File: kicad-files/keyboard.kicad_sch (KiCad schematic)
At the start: 180 parts, among them J1 TYPE-C-31-M12_13, Q1 2N7002, Q2 2N7002, SW1 K2-1187SQ-A4SW-06, U1 STM32F411CEU6, U2 USBLC6-2SC6, U3 AT24C256C-SSHL-T, U4 SGM2007-3.3XN5/TR, Y1 TAXM8M4RFDCET2T

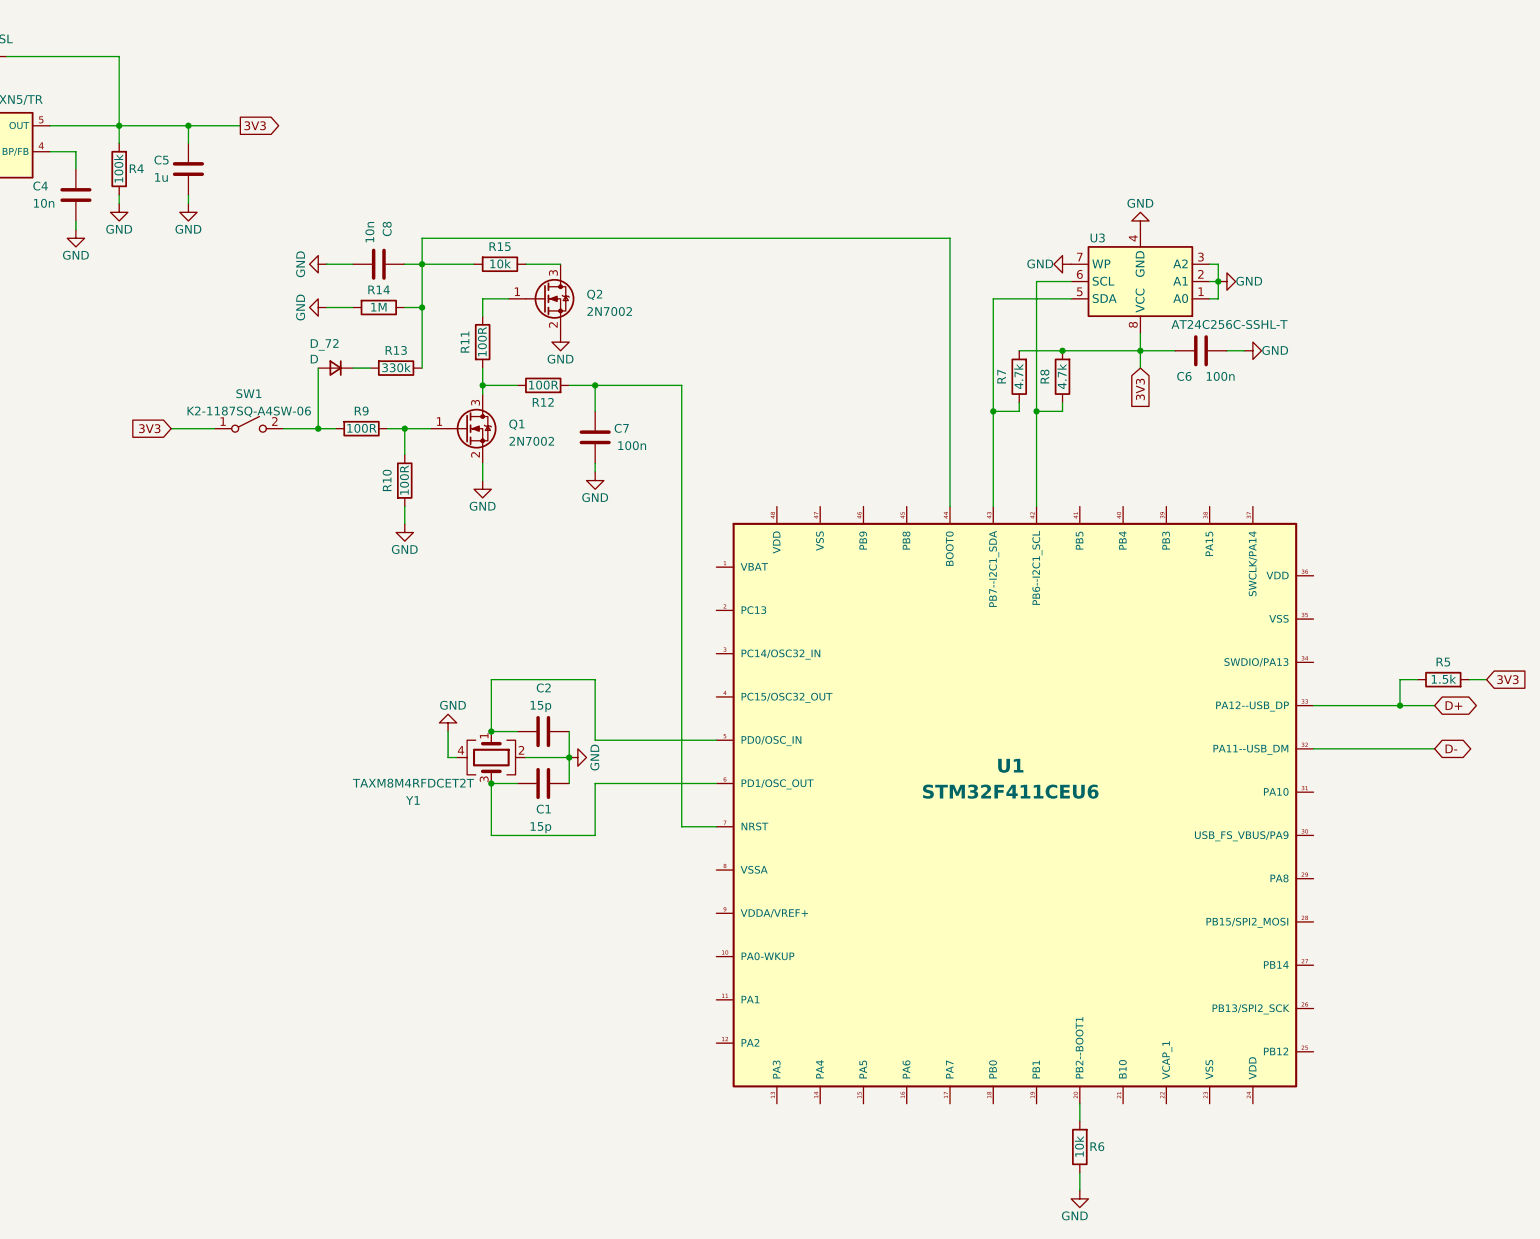
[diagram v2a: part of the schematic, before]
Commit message: Added 3V3 connections to controller
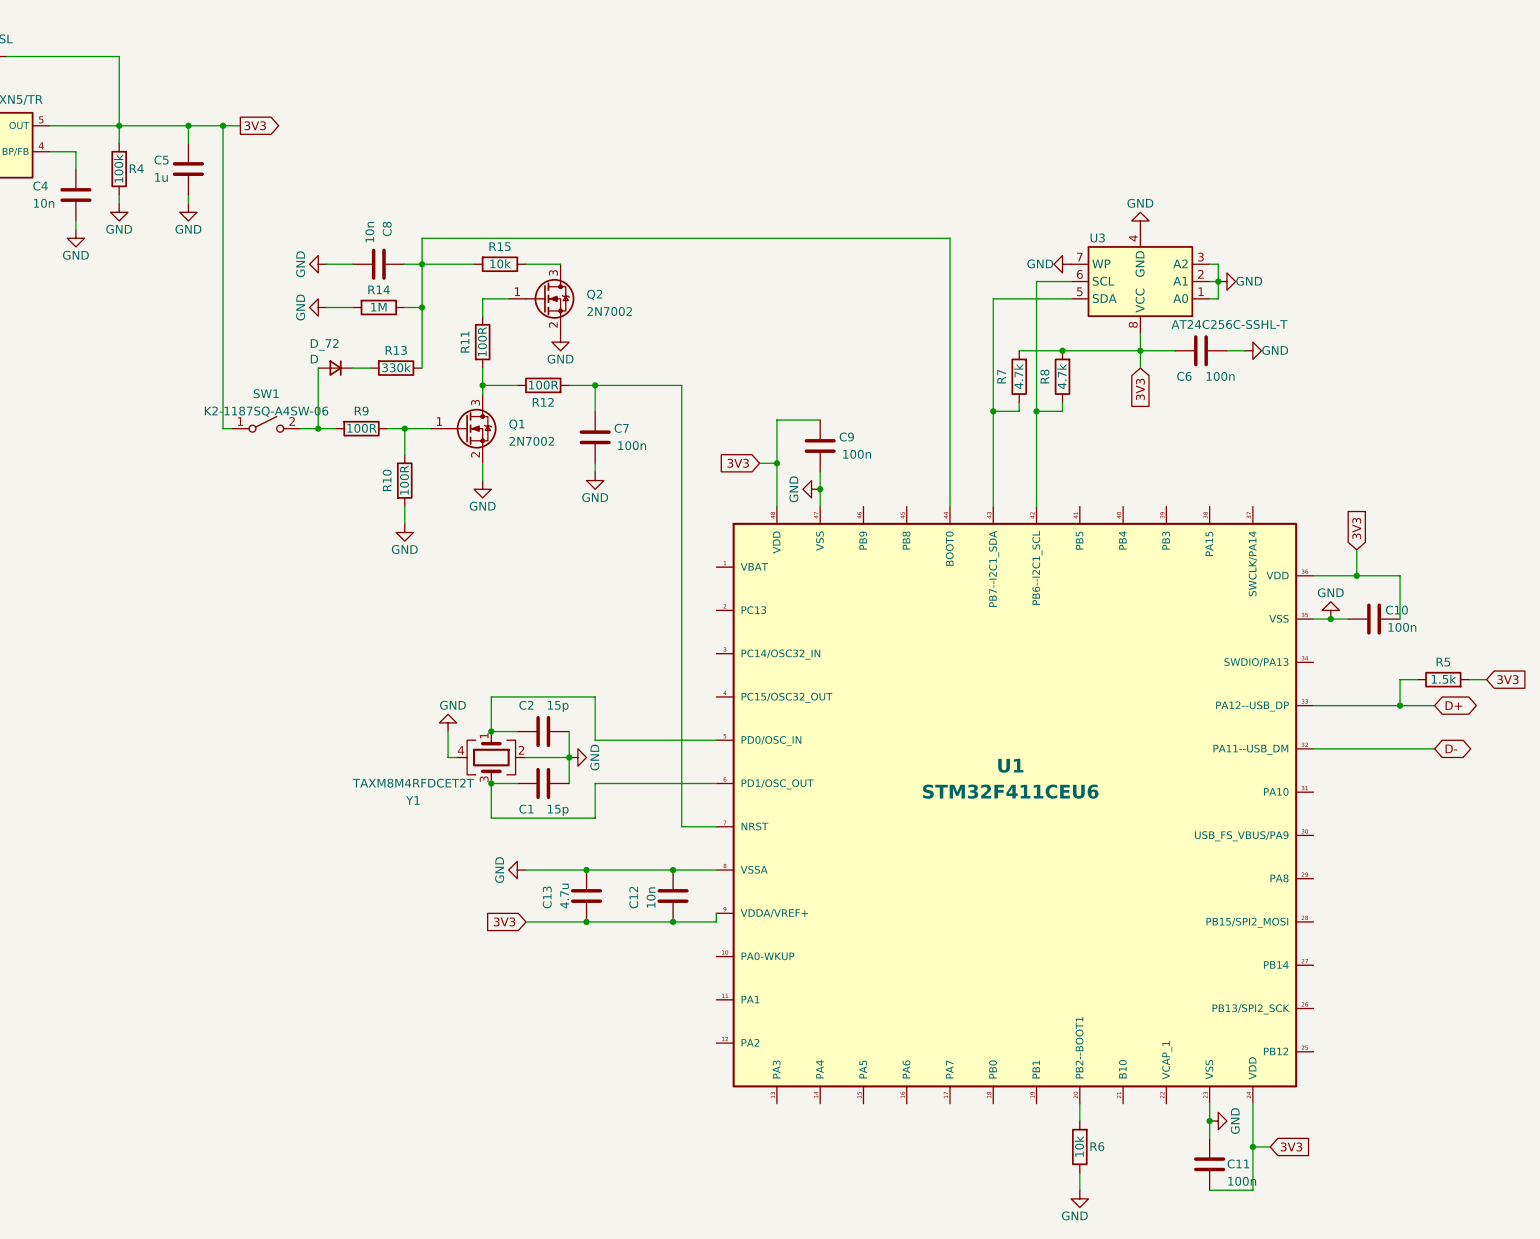
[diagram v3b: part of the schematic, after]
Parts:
- added C10, C11, C9: 100n, Capacitor_SMD:C_0603_1608Metric_Pad1.08x0.95mm_HandSolder, symbol Device:C
- added C12: 10n, Capacitor_SMD:C_0603_1608Metric_Pad1.08x0.95mm_HandSolder, symbol Device:C
- added C13: 4.7u, Capacitor_SMD:C_0603_1608Metric_Pad1.08x0.95mm_HandSolder, symbol Device:C
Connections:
- net 3V3: now also U1.24 (VDD), U1.36 (VDD), U1.48 (VDD), U1.9 (VDDA/VREF+), C10.2, C11.2, C12.2, C13.2, C9.2
- net GND: now also U1.23 (VSS), U1.35 (VSS), U1.47 (VSS), U1.8 (VSSA), C10.1, C11.1, C12.1, C13.1, C9.1
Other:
- moved on the sheet: SW1

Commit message: Connected pulldown for 3V3 on the STM
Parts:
- U1: footprint acheron_Components:STM_UFQFPN-48_LQFP-48-1EP_7x7mm_P0.5mm_HandSoldering_ThermalReliefs -> acheron_Components:STM_UFQFPN-48_LQFP-48-1EP_7x7mm_P0.5mm_HandSoldering
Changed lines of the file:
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@@
       (effects (font (size 2.0066 2.0066) bold))
     )
-    (property "Footprint" "acheron_Components:STM_UFQFPN-48_LQFP-48-1EP_7x7mm_P0.5mm_HandSoldering_ThermalReliefs" (at 307.34 330.2 0)
+    (property "Footprint" "acheron_Components:STM_UFQFPN-48_LQFP-48-1EP_7x7mm_P0.5mm_HandSoldering" (at 307.34 330.2 0)
       (effects (font (size 1.27 1.27)) hide)
     )

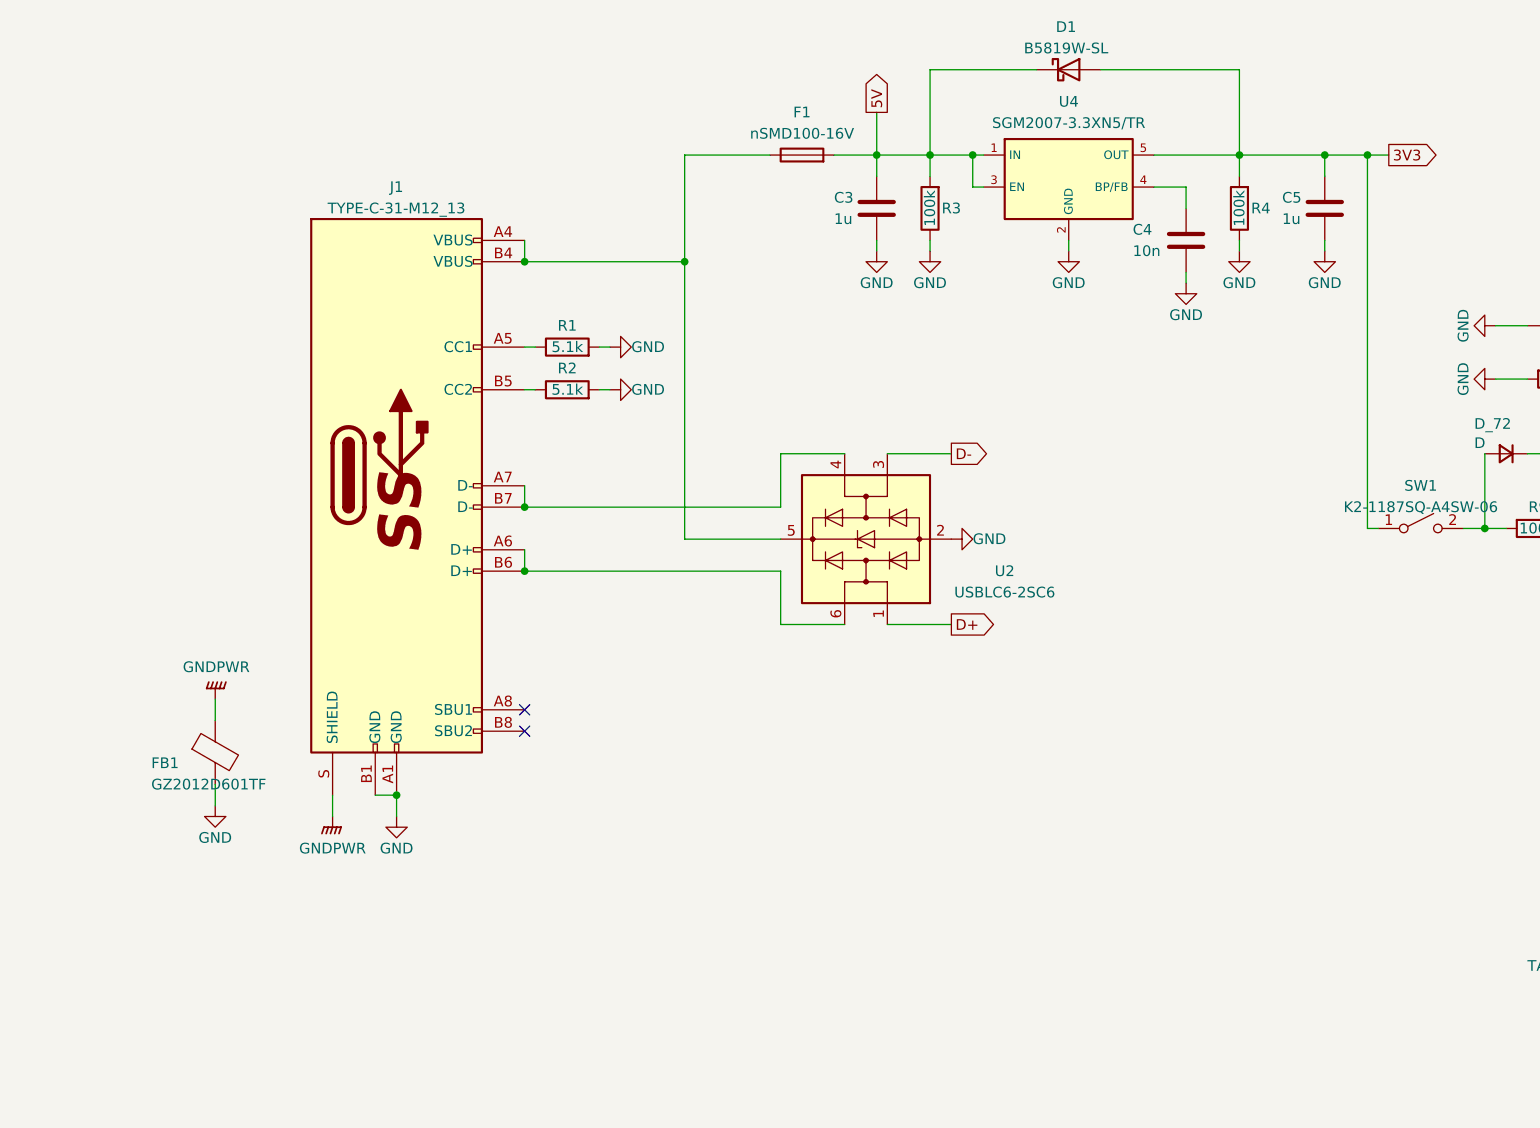
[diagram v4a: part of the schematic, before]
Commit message: Added connector for DB
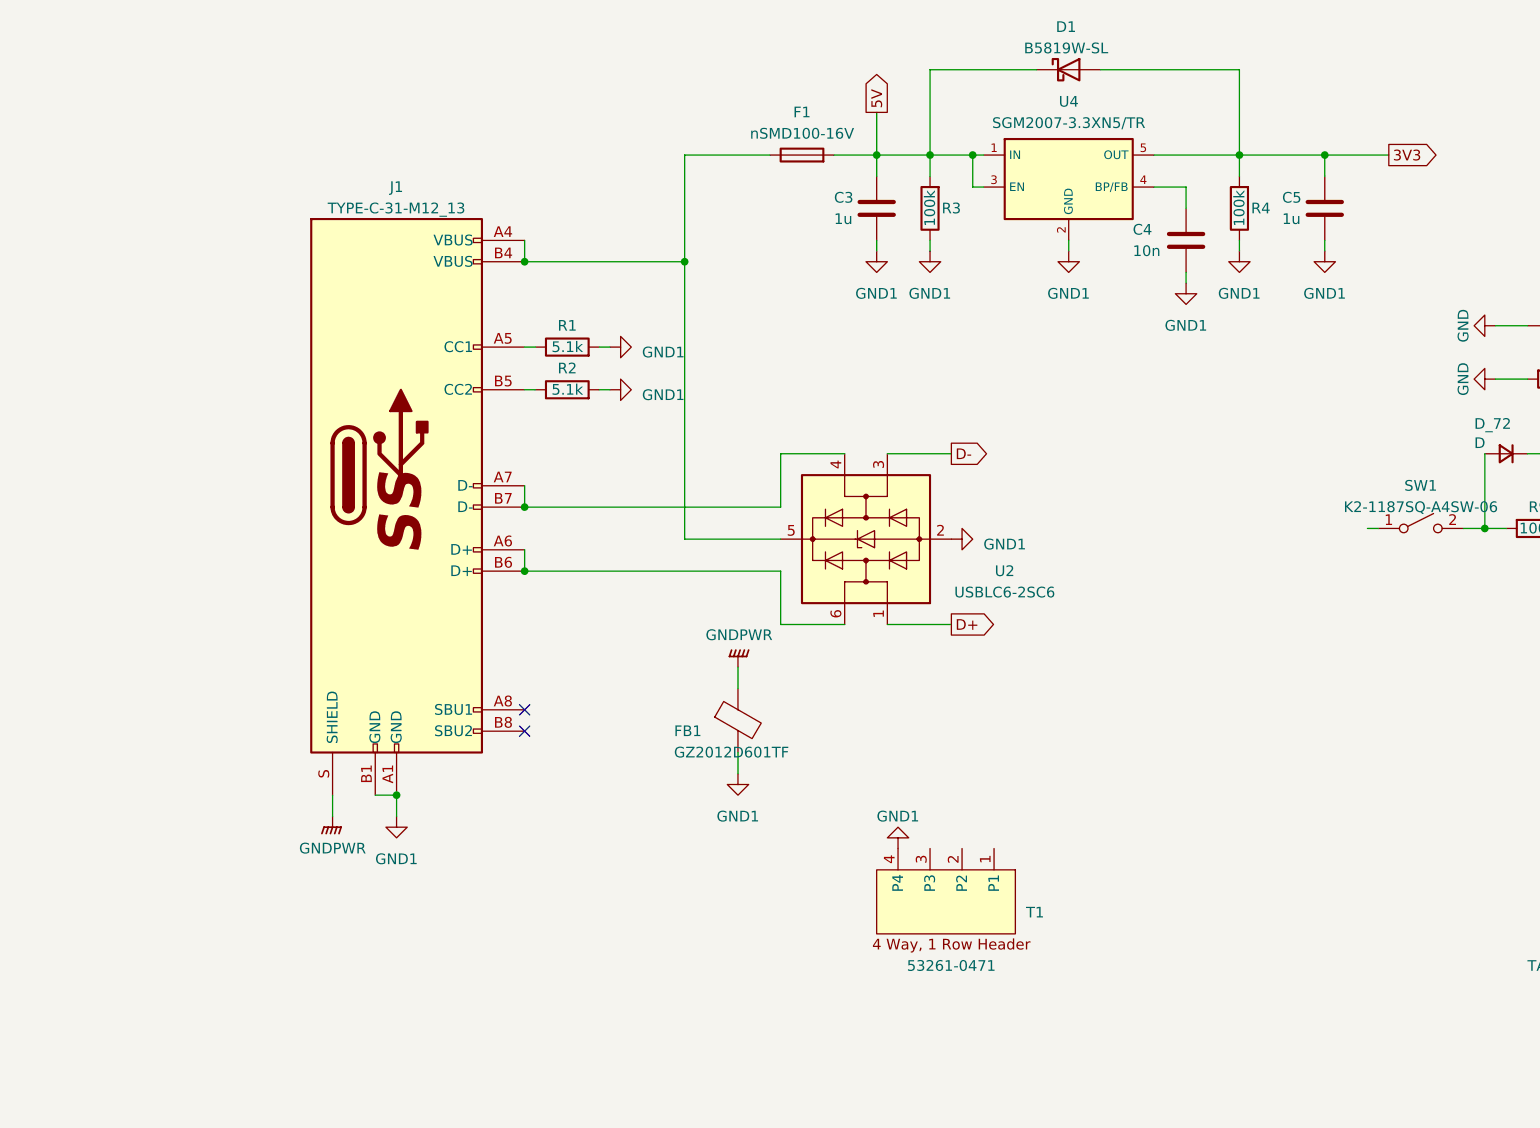
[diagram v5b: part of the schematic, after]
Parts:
- added T1: 53261-0471, Legshark:Molex, PicoBlade, 53261, 4 Way, 1 Row, Right Angle PCB Header, symbol legshark_symbols:Header_4_Way,_1_Row
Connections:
- net 3V3: no longer SW1.1 (A)
- net GND: no longer C3.2, C4.2, C5.2, FB1.2, J1.A1 (GND), J1.B1 (GND), R1.2, R2.2, R3.1, R4.1, U2.2 (GND), U4.2 (GND)
- new net GND1: C3.2, C4.2, C5.2, FB1.2, J1.A1 (GND), J1.B1 (GND), R1.2, R2.2, R3.1, R4.1, T1.4 (P4), U2.2 (GND), U4.2 (GND)
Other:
- moved on the sheet: FB1

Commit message: Added the cable header for DB to MB
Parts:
- added T2: 53261-0471, Legshark:Molex, PicoBlade, 53261, 4 Way, 1 Row, Right Angle PCB Header, symbol legshark_symbols:Header_4_Way,_1_Row
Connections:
- net 3V3: now also SW1.1 (A), T2.1 (3V3); no longer C5.1, D1.2 (A), R4.2, U4.5 (OUT)
- net D+: now also T2.3 (D+); no longer U2.1 (I/O1)
- net D-: now also T2.2 (D-); no longer U2.3 (I/O2)
- net GND: now also T2.4 (GND)
- net at T1.1 (3V3): now also C5.1, D1.2 (A), R4.2, U4.5 (OUT)
- net at T1.2 (D-): now also U2.3 (I/O2)
- net at T1.3 (D+): now also U2.1 (I/O1)
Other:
- moved on the sheet: C1, C10, C11, C12, C13, C2, C3, C4, C5, C6, C7, C8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
